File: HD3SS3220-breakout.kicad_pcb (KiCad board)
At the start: 4 copper layers, 29 x 53.3 mm, 35 parts, among them J1 USB_C_Receptacle, J2 U-A-39SS-Y-1, J3 A2541WV-2x4P, SW1 DSHP06TSGER_C3293146, U1 HD3SS3220RNHR, U2 TPD4EUSB30, U3 TPD4EUSB30, U4 TPD4EUSB30, U5 HT7533-1_C14289

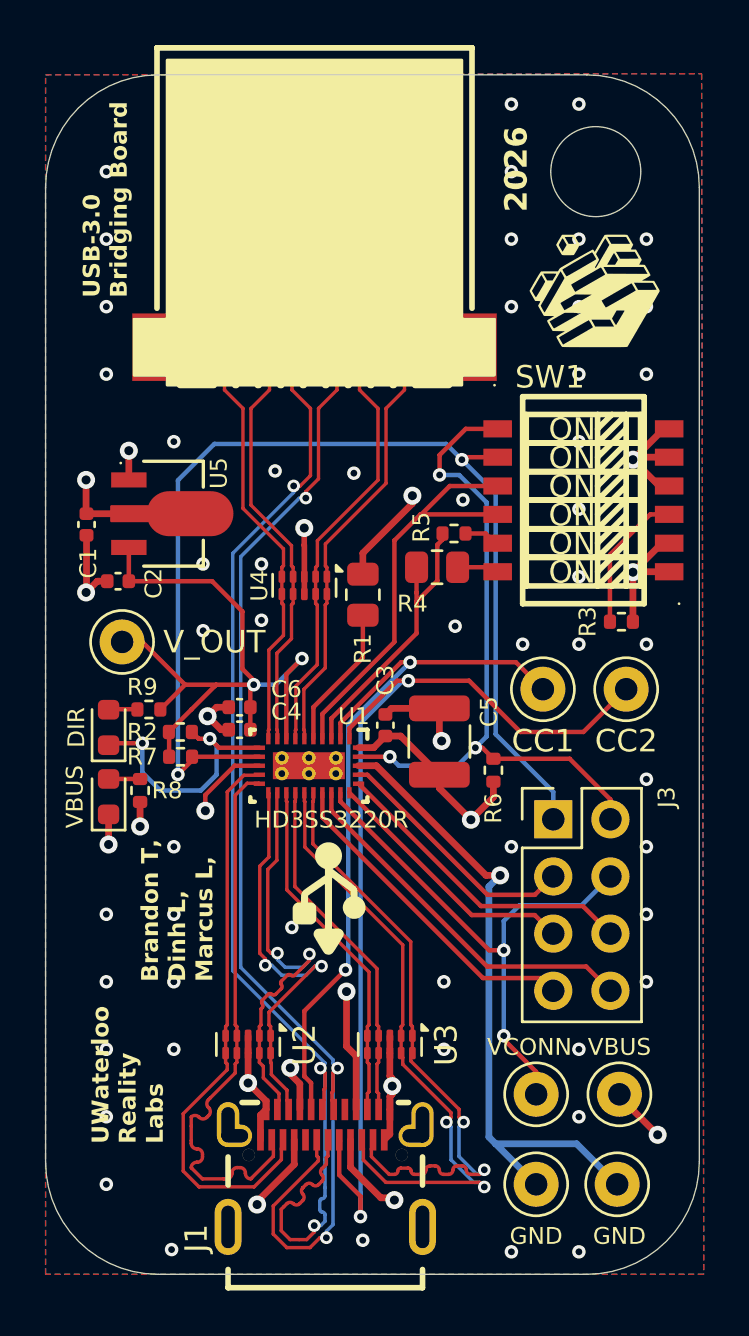
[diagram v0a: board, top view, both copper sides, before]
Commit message: Footprint and symbol fix
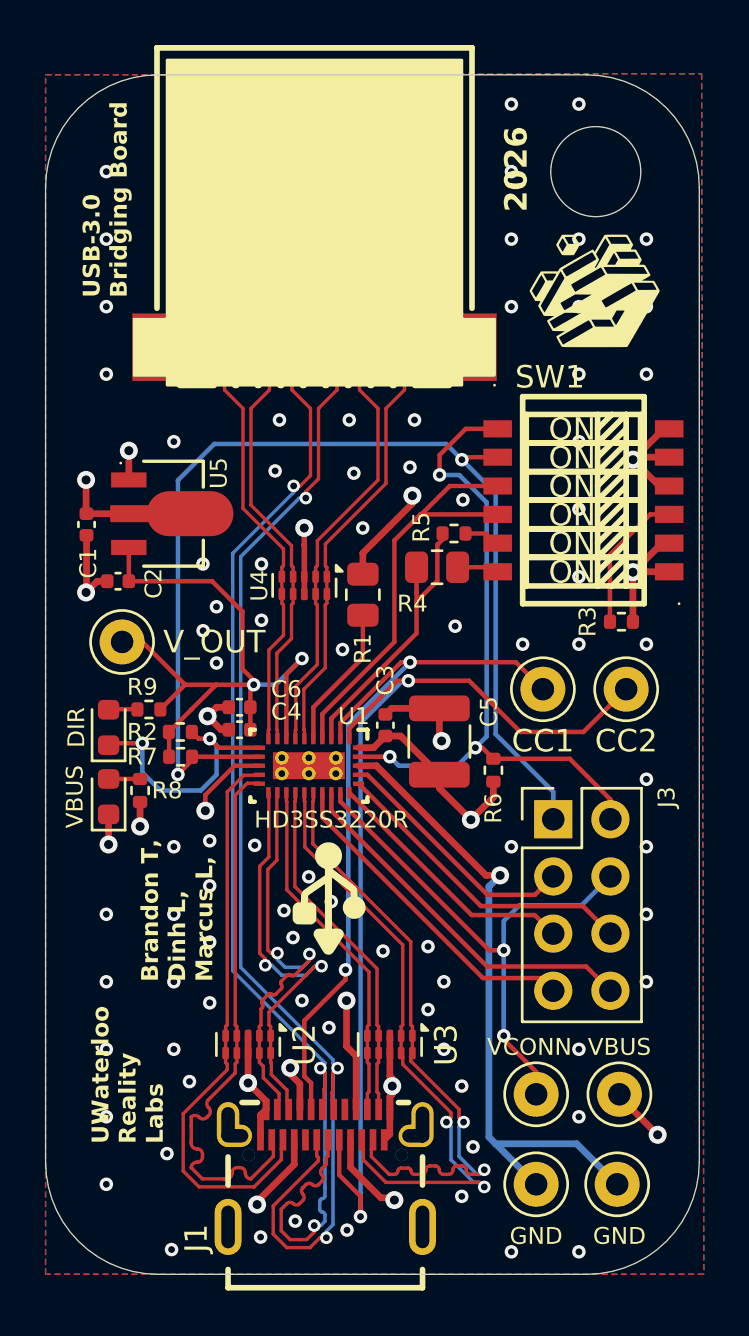
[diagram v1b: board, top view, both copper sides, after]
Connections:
- C1 pad 1: GND -> VBUS
- C3 pad 2: GND -> VBUS
- C5 pad 2: GND -> VBUS
- J1 pad 1: (no net) -> GND
- J1 pad 2: (no net) -> GND
- J1 pad 3: (no net) -> GND
- J1 pad 4: (no net) -> GND
- J1 pad A4: GND -> VBUS
- J1 pad A9: GND -> VBUS
- J1 pad B4: GND -> VBUS
- J1 pad B9: GND -> VBUS
- J2 pad 1: GND -> VBUS
- R1 pad 1: GND -> VBUS
- R3 pad 1: GND -> VBUS
- R6 pad 1: GND -> VBUS
- R8 pad 1: GND -> VBUS
- SW1 pad 1: GND -> VBUS
- SW1 pad 2: GND -> VBUS
- U1 pad 30: GND -> VBUS
- U5 pad 2: GND -> VBUS
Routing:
- net GND: track 109.1 -> 64.3 mm, vias 89 -> 105
- net VBUS: track 2.50 -> 47.0 mm, vias 2 -> 12
- net (no net): vias 0 -> 2

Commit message: Re-annotate 9 clobbered PCB refs (TP1-7, DIR_LED2, VBUS_LED2) by symbol UUID
Refs had been overwritten with net-style names (GND x2, VBUS x2, CC1, CC2,
DIR, VCONN, V_OUT), giving 9 missing + 9 extra + 2 duplicate schematic-parity
violations and blocking netlist sync / CPL generation. Footprint path UUIDs
already pointed at the correct symbols; only the Reference properties are
changed. Parity now reports 0 issues.
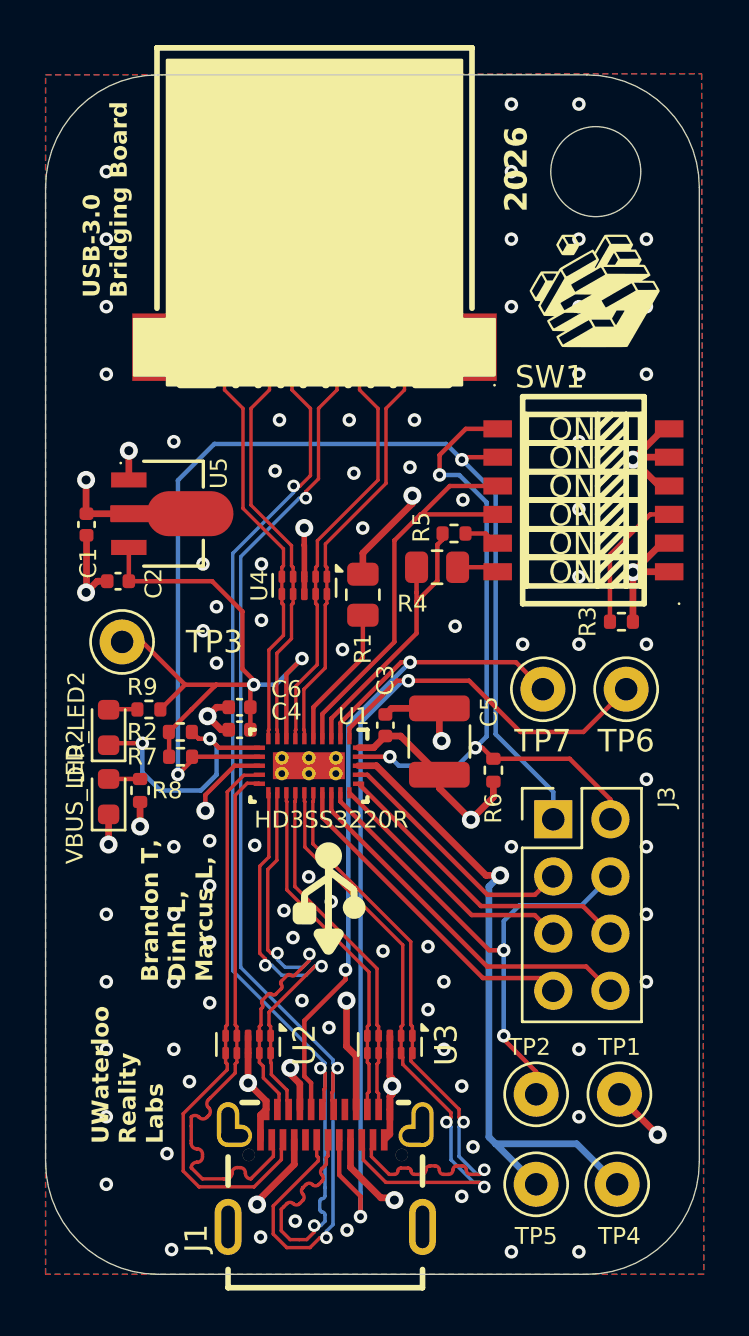
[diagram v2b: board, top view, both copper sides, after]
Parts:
- renumbered DIR to DIR_LED2, VBUS to TP1, VCONN to TP2, V_OUT to TP3, GND to TP4, GND to TP5, CC2 to TP6, CC1 to TP7, VBUS to VBUS_LED2
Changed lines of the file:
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@@
 		(descr "Keystone THM Miniature Test Point 5000-5004, http://www.keyelco.com/product-pdf.cfm?p=1309")
 		(tags "Through Hole Mount Test Points")
-		(property "Reference" "GND"
+		(property "Reference" "TP5"
 			(at 0 2.3 180)
 			(layer "F.SilkS")
@@
 		(descr "Keystone THM Miniature Test Point 5000-5004, http://www.keyelco.com/product-pdf.cfm?p=1309")
 		(tags "Through Hole Mount Test Points")
-		(property "Reference" "CC2"
+		(property "Reference" "TP6"
 			(at 0 2.3 0)
 			(layer "F.SilkS")
@@
 		(descr "Keystone THM Miniature Test Point 5000-5004, http://www.keyelco.com/product-pdf.cfm?p=1309")
 		(tags "Through Hole Mount Test Points")
-		(property "Reference" "V_OUT"
+		(property "Reference" "TP3"
 			(at 4.1 0 0)
 			(layer "F.SilkS")
@@
 		(descr "Keystone THM Miniature Test Point 5000-5004, http://www.keyelco.com/product-pdf.cfm?p=1309")
 		(tags "Through Hole Mount Test Points")
-		(property "Reference" "GND"
+		(property "Reference" "TP4"
 			(at 0.1 2.3 180)
 			(layer "F.SilkS")
@@
 		(descr "LED SMD 0603 (1608 Metric), square (rectangular) end terminal, IPC-7351 nominal, (Body size source: http://www.tortai-tech.com/upload/download/2011102023233369053.pdf)")
 		(tags "LED")
-		(property "Reference" "DIR"
+		(property "Reference" "DIR_LED2"
 			(at 0 -1.43 90)
 			(layer "F.SilkS")
@@
 		(descr "Keystone THM Miniature Test Point 5000-5004, http://www.keyelco.com/product-pdf.cfm?p=1309")
 		(tags "Through Hole Mount Test Points")
-		(property "Reference" "VCONN"
+		(property "Reference" "TP2"
 			(at -0.3 -2.1 180)
 			(layer "F.SilkS")
@@
 		(descr "Keystone THM Miniature Test Point 5000-5004, http://www.keyelco.com/product-pdf.cfm?p=1309")
 		(tags "Through Hole Mount Test Points")
-		(property "Reference" "CC1"
+		(property "Reference" "TP7"
 			(at 0 2.3 0)
 			(layer "F.SilkS")
@@
 		(descr "LED SMD 0603 (1608 Metric), square (rectangular) end terminal, IPC-7351 nominal, (Body size source: http://www.tortai-tech.com/upload/download/2011102023233369053.pdf)")
 		(tags "LED")
-		(property "Reference" "VBUS"
+		(property "Reference" "VBUS_LED2"
 			(at 0 -1.5 270)
 			(layer "F.SilkS")
@@
 		(descr "Keystone THM Miniature Test Point 5000-5004, http://www.keyelco.com/product-pdf.cfm?p=1309")
 		(tags "Through Hole Mount Test Points")
-		(property "Reference" "VBUS"
+		(property "Reference" "TP1"
 			(at 0 -2.1 0)
 			(layer "F.SilkS")

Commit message: Add In2 GND reference patches + return vias under TX1/TX2 crossovers
TX1/TX2 each do a polarity crossover (U1 pad order is inverted vs J1), so
their B.Cu under-passes are topologically unavoidable - but they referenced
the In2 VBUS plane with no return path (r5 must-fix).

- Two GND zones on In2 (priority 2) under the crossover regions, so the
  B.Cu sections reference GND instead of VBUS end to end.
- 7 GND return vias adjacent to the 8 signal vias (0.6/0.3); the TX1-
  entry via has no room for a dedicated one (D+/D- run on B.Cu 0.85 mm
  west) and shares the cluster's return path.
- Patches sized to swallow two pre-existing GND stitch vias whose pads
  kissed the first-cut patch edge (zero-width connection warnings).
- D+/D- B.Cu diagonals cross the TX1 patch edge for ~1-2 mm: two extra
  reference transitions at 480 Mb/s, benign; the GND stretch is a better
  reference than the VBUS plane it replaces.

DRC: parity clean, 0 unconnected, no new errors (9 pre-existing J1
footprint-internal hole_clearance remain).
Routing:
- net GND: vias 105 -> 112
- added copper zone on In2.Cu, net GND
